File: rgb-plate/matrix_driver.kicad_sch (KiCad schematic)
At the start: 27 parts, among them J1 Conn_01x09, U1 TPS562202, U2 LP5891MRRFR, U3 TPS562202

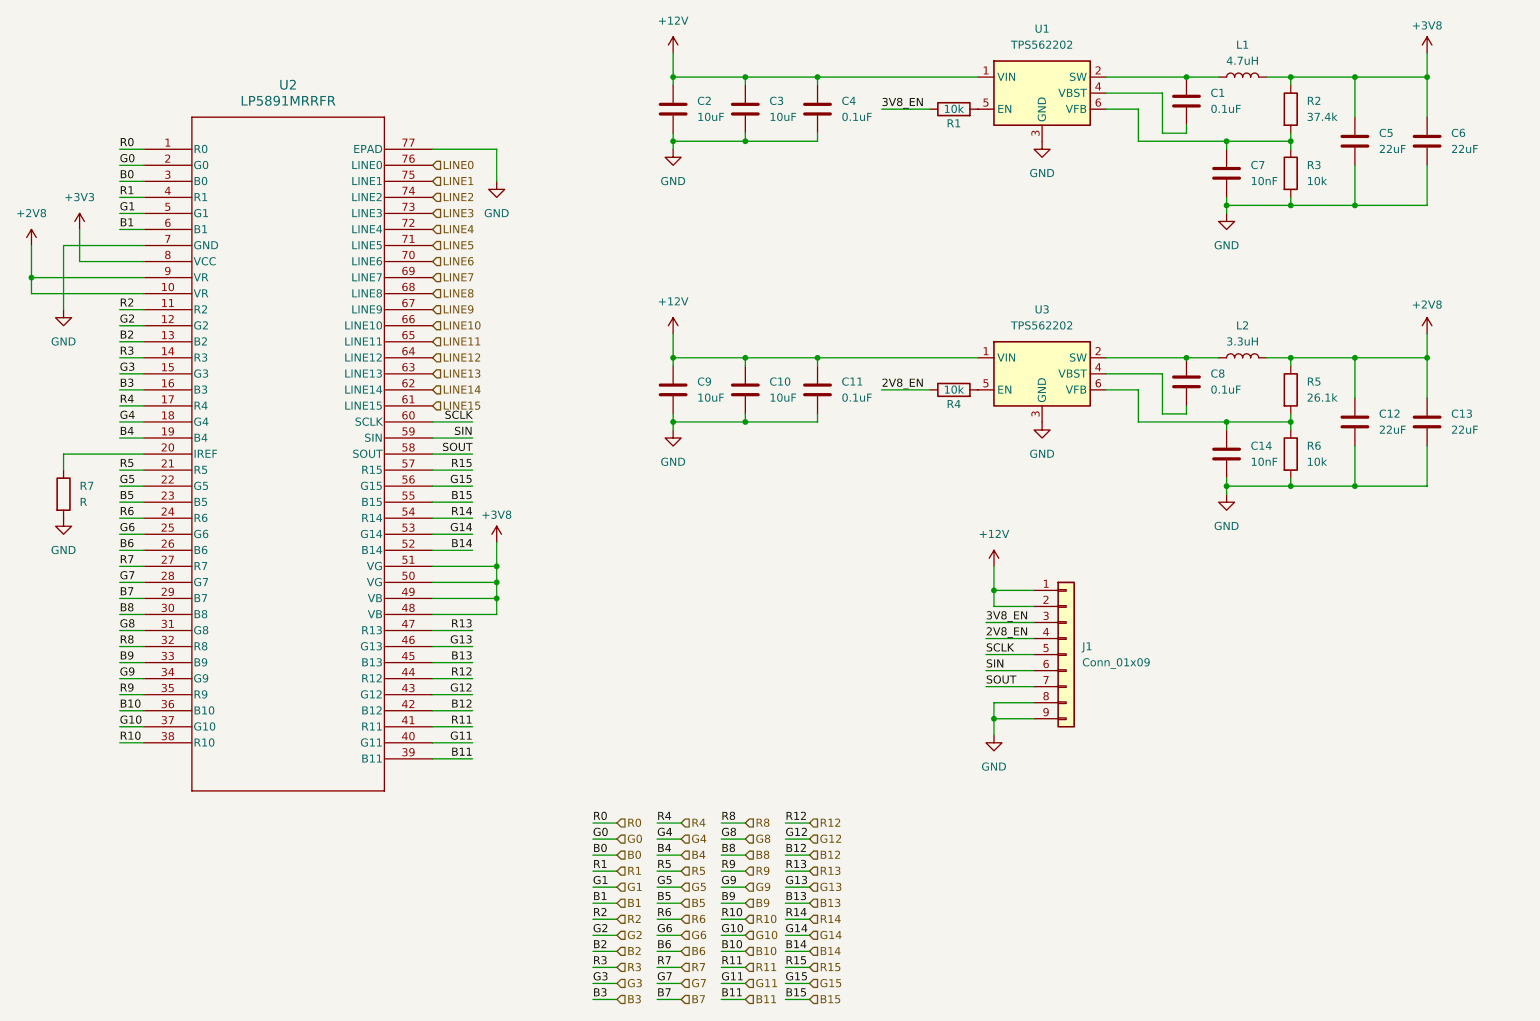
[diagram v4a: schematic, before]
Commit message: update complete architecture to allow for improved routing scheme - separate boards for led plate and driver. adjusted matrix board to only hold leds and connectors and thermistors, created new board for driver
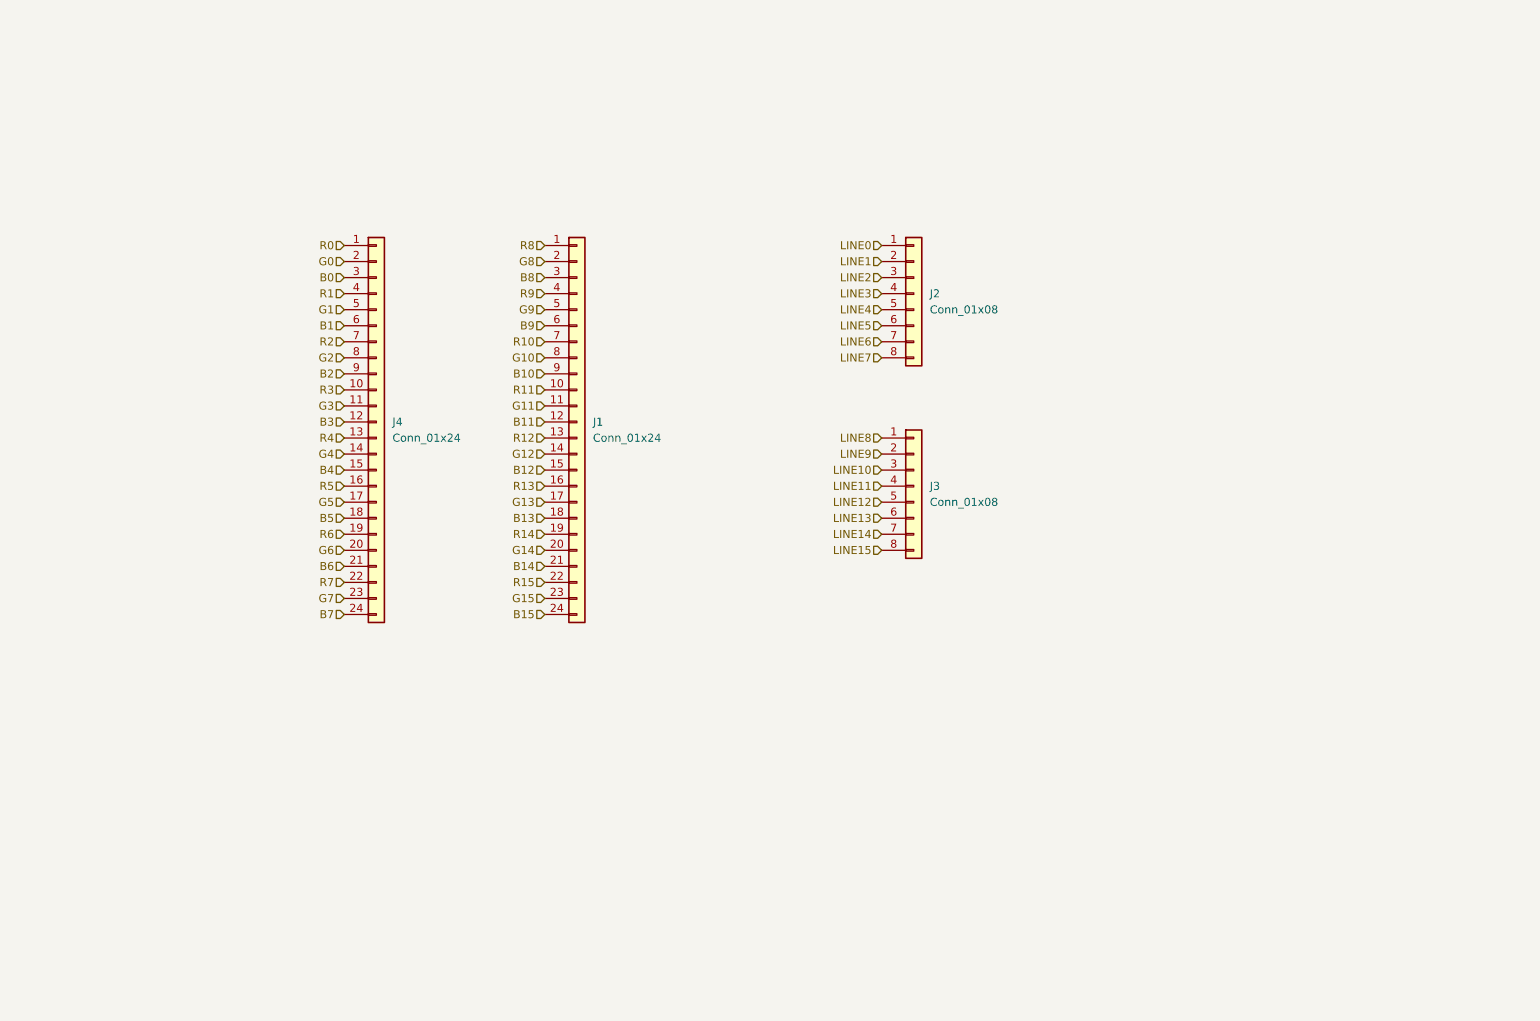
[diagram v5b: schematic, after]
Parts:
- removed C1, C11, C4, C8: 0.1uF, Capacitor_SMD:C_0603_1608Metric, symbol Device:C
- removed C10, C2, C3, C9: 10uF, Capacitor_SMD:C_1206_3216Metric, symbol Device:C
- removed C12, C13, C5, C6: 22uF, Capacitor_SMD:C_1206_3216Metric, symbol Device:C
- removed C14, C7: 10nF, Capacitor_SMD:C_0603_1608Metric, symbol Device:C
- removed J1: Conn_01x09, symbol Connector_Generic:Conn_01x09
- removed L1: 4.7uH, symbol Device:L
- removed L2: 3.3uH, symbol Device:L
- removed R1, R3, R4, R6: 10k, Resistor_SMD:R_0603_1608Metric, symbol Device:R
- removed R2: 37.4k, Resistor_SMD:R_0603_1608Metric, symbol Device:R
- removed R5: 26.1k, Resistor_SMD:R_0603_1608Metric, symbol Device:R
- removed R7: R, Resistor_SMD:R_0603_1608Metric, symbol Device:R
- removed U1, U3: TPS562202, Package_TO_SOT_SMD:SOT-563, symbol Regulator_Switching:TPS562202
- removed U2: LP5891MRRFR, ul_LP5891MRRFR:VQFN76_RRF_TEX, symbol ul_LP5891MRRFR:LP5891MRRFR
- added J1, J4: Conn_01x24, symbol Connector_Generic:Conn_01x24
- added J2, J3: Conn_01x08, symbol Connector_Generic:Conn_01x08
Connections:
- net B0: now also J4.3 (Pin_3)
- net B1: now also J4.6 (Pin_6)
- net B10: now also J1.9 (Pin_9)
- net B11: now also J1.12 (Pin_12)
- net B12: now also J1.15 (Pin_15)
- net B13: now also J1.18 (Pin_18)
- net B14: now also J1.21 (Pin_21)
- net B15: now also J1.24 (Pin_24)
- net B2: now also J4.9 (Pin_9)
- net B3: now also J4.12 (Pin_12)
- net B4: now also J4.15 (Pin_15)
- net B5: now also J4.18 (Pin_18)
- net B6: now also J4.21 (Pin_21)
- net B7: now also J4.24 (Pin_24)
- net B8: now also J1.3 (Pin_3)
- net B9: now also J1.6 (Pin_6)
- net G0: now also J4.2 (Pin_2)
- net G1: now also J4.5 (Pin_5)
- net G10: now also J1.8 (Pin_8)
- net G11: now also J1.11 (Pin_11)
- net G12: now also J1.14 (Pin_14)
- net G13: now also J1.17 (Pin_17)
- net G14: now also J1.20 (Pin_20)
- net G15: now also J1.23 (Pin_23)
- net G2: now also J4.8 (Pin_8)
- net G3: now also J4.11 (Pin_11)
- net G4: now also J4.14 (Pin_14)
- net G5: now also J4.17 (Pin_17)
- net G6: now also J4.20 (Pin_20)
- net G7: now also J4.23 (Pin_23)
- net G8: now also J1.2 (Pin_2)
- net G9: now also J1.5 (Pin_5)
- net LINE0: now also J2.1 (Pin_1)
- net LINE1: now also J2.2 (Pin_2)
- net LINE10: now also J3.3 (Pin_3)
- net LINE11: now also J3.4 (Pin_4)
- net LINE12: now also J3.5 (Pin_5)
- net LINE13: now also J3.6 (Pin_6)
- net LINE14: now also J3.7 (Pin_7)
- net LINE15: now also J3.8 (Pin_8)
- net LINE2: now also J2.3 (Pin_3)
- net LINE3: now also J2.4 (Pin_4)
- net LINE4: now also J2.5 (Pin_5)
- net LINE5: now also J2.6 (Pin_6)
- net LINE6: now also J2.7 (Pin_7)
- net LINE7: now also J2.8 (Pin_8)
- net LINE8: now also J3.1 (Pin_1)
- net LINE9: now also J3.2 (Pin_2)
- net R0: now also J4.1 (Pin_1)
- net R1: now also J4.4 (Pin_4)
- net R10: now also J1.7 (Pin_7)
- net R11: now also J1.10 (Pin_10)
- net R12: now also J1.13 (Pin_13)
- net R13: now also J1.16 (Pin_16)
- net R14: now also J1.19 (Pin_19)
- net R15: now also J1.22 (Pin_22)
- net R2: now also J4.7 (Pin_7)
- net R3: now also J4.10 (Pin_10)
- net R4: now also J4.13 (Pin_13)
- net R5: now also J4.16 (Pin_16)
- net R6: now also J4.19 (Pin_19)
- net R7: now also J4.22 (Pin_22)
- net R8: now also J1.1 (Pin_1)
- net R9: now also J1.4 (Pin_4)
